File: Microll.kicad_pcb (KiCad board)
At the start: 2 copper layers, 22 parts, among them J1 USB_C_Receptacle, U1 ESP32-C3-WROOM-02-N4, U2 TLV76733DRVx, U3 STM32G0B1CBU6, U4 USBLC6-2P6, U5 DPDT_Switch_x2, U6 LSM6DSL

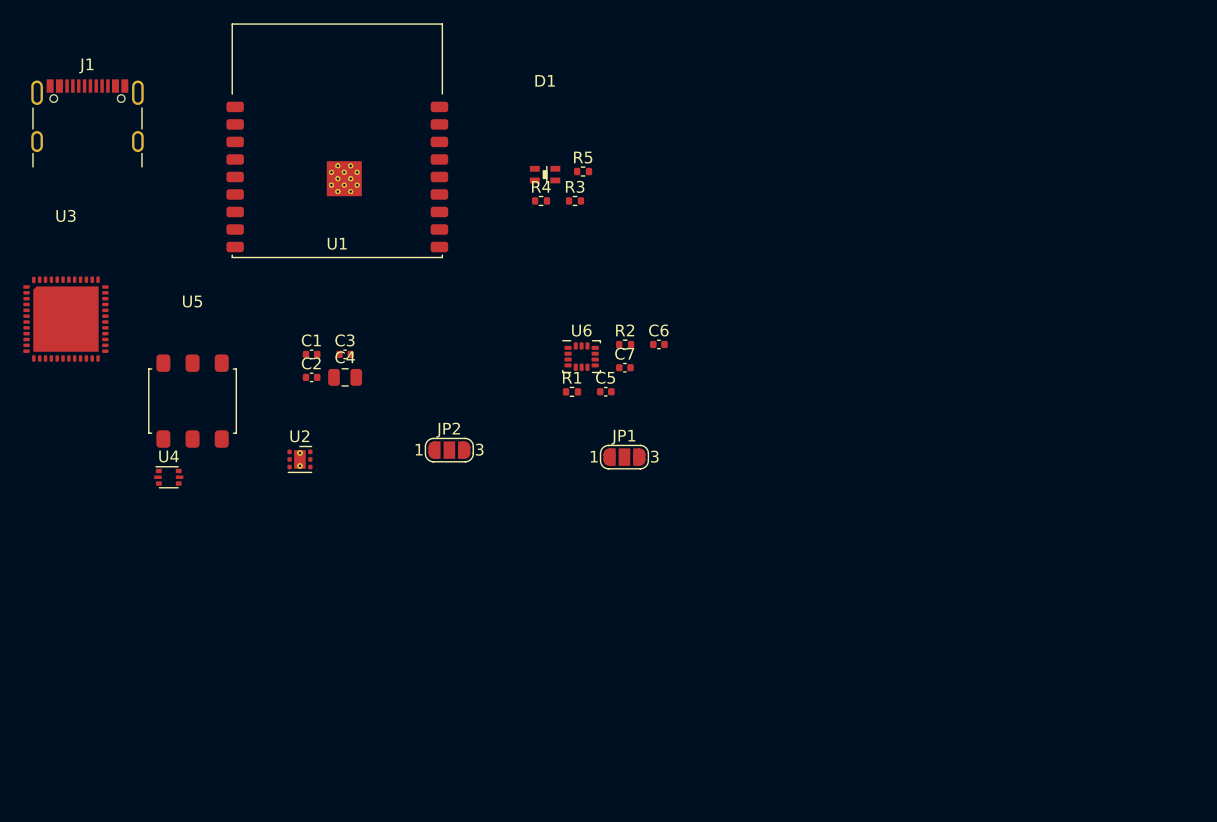
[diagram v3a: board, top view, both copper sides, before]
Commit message: Added I/O connections
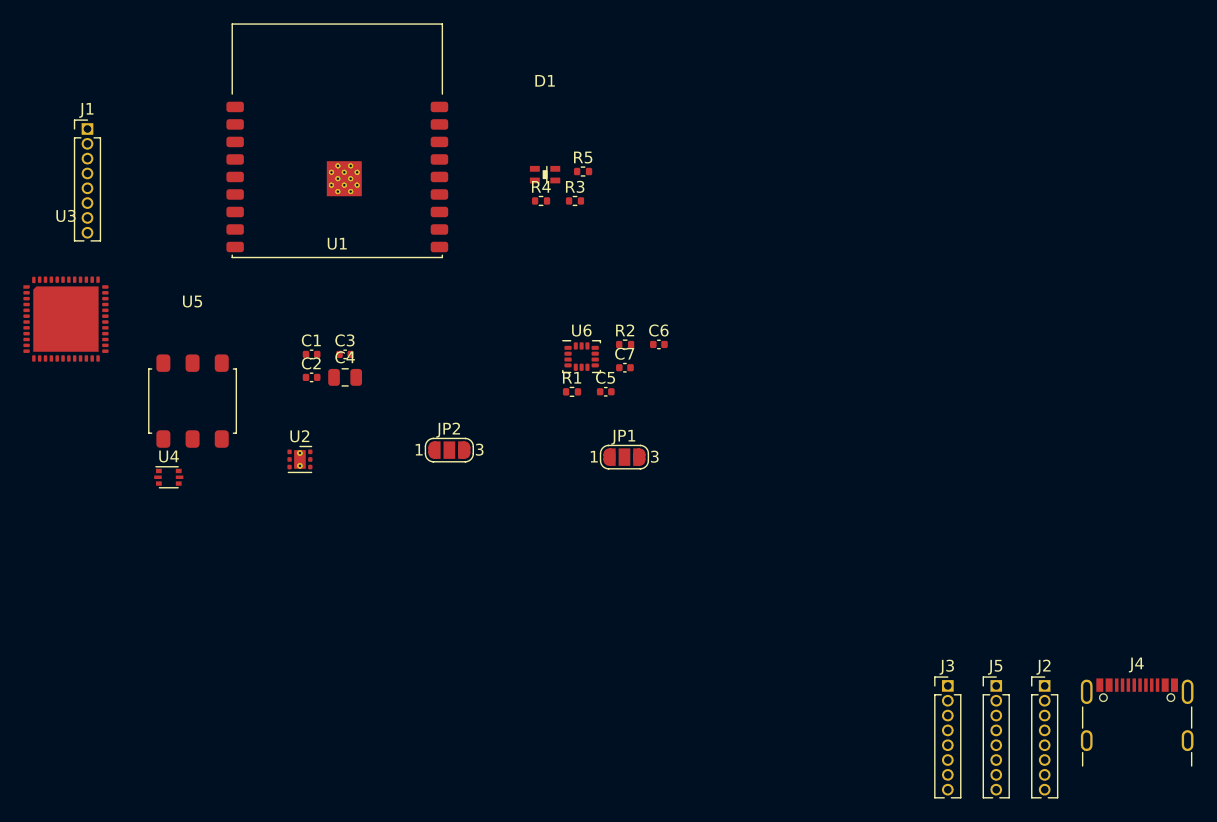
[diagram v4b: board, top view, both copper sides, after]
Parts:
- added J2: Conn_01x08, Connector_PinHeader_1.27mm:PinHeader_1x08_P1.27mm_Vertical, F.Cu at (222.0, 122.8)
- added J3: Conn_01x08, Connector_PinHeader_1.27mm:PinHeader_1x08_P1.27mm_Vertical, F.Cu at (213.7, 122.8)
- added J4: USB_C_Receptacle, Connector_USB:USB_C_Receptacle_GCT_USB4105-xx-A_16P_TopMnt_Horizontal, F.Cu at (229.9, 126.4)
- added J5: Conn_01x08, Connector_PinHeader_1.27mm:PinHeader_1x08_P1.27mm_Vertical, F.Cu at (217.8, 122.8)
- J1: value USB_C_Receptacle -> Conn_01x08; footprint Connector_USB:USB_C_Receptacle_GCT_USB4105-xx-A_16P_TopMnt_Horizontal -> Connector_PinHeader_1.27mm:PinHeader_1x08_P1.27mm_Vertical
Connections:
- U1 pad 10: unconnected-(U1-Pad10) -> /GPIO10
- U1 pad 11: unconnected-(U1-Pad11) -> /Rx
- U1 pad 12: unconnected-(U1-Pad12) -> /Tx
- U1 pad 15: unconnected-(U1-Pad15) -> /GPIO3
- U1 pad 16: unconnected-(U1-Pad16) -> /GPIO2
- U1 pad 17: unconnected-(U1-Pad17) -> /GPIO1
- U1 pad 18: unconnected-(U1-Pad18) -> /Blue
- U1 pad 6: unconnected-(U1-Pad6) -> /GPIO7
- U1 pad 7: unconnected-(U1-Pad7) -> /GPIO8
- U3 pad 13: unconnected-(U3-Pad13) -> /PA2
- U3 pad 14: unconnected-(U3-Pad14) -> /PA3
- U3 pad 19: unconnected-(U3-Pad19) -> /PB0
- U3 pad 20: unconnected-(U3-Pad20) -> /PB1
- U3 pad 25: unconnected-(U3-Pad25) -> /PB13
- U3 pad 26: unconnected-(U3-Pad26) -> /PB14
- U3 pad 27: unconnected-(U3-Pad27) -> /PB15
- U3 pad 28: unconnected-(U3-Pad28) -> /PA8
- U3 pad 41: unconnected-(U3-Pad41) -> /PD3
- U3 pad 42: unconnected-(U3-Pad42) -> /PB3
- U3 pad 43: unconnected-(U3-Pad43) -> /PB4
- U3 pad 44: unconnected-(U3-Pad44) -> /PB5

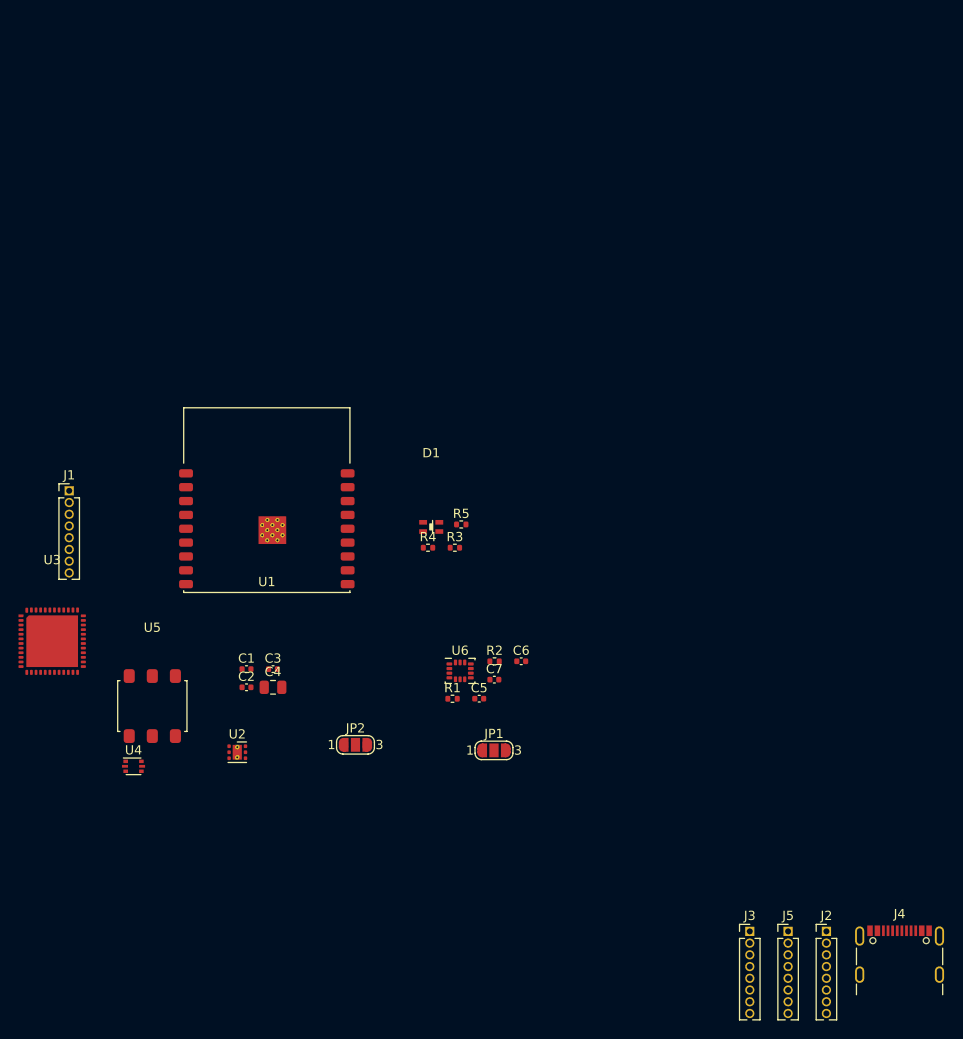
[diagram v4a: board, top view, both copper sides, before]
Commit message: Initial placement for the PCB.
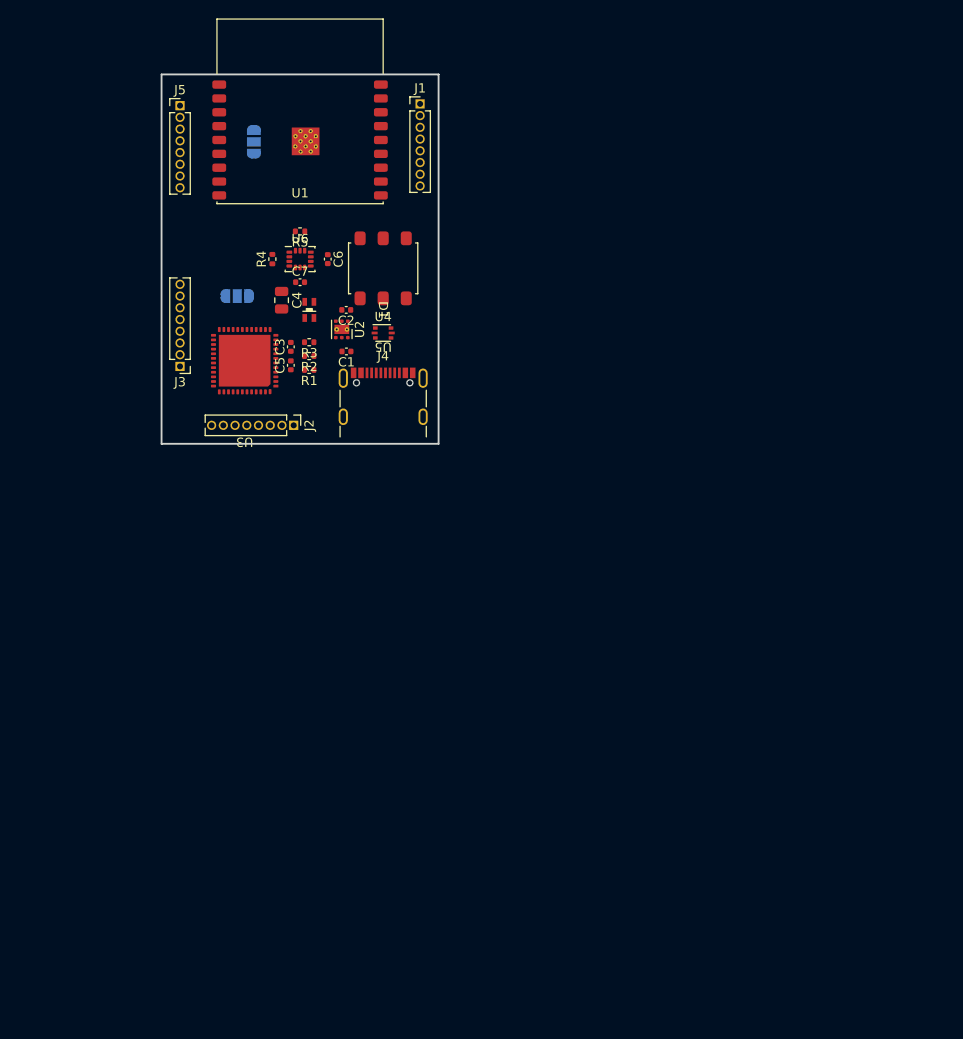
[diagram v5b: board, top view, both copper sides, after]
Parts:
- JP1, JP2: moved to B.Cu
- moved J5 111.1 mm to (152.0, 33.4)
- moved J3 86.9 mm to (152.0, 61.6), turned to 180 degrees
- moved J4 82.3 mm to (174.0, 66.0)
- moved J2 79.6 mm to (164.3, 68.0), turned to -90 degrees
- moved JP1 70.8 mm to (160.0, 37.3), turned to -90 degrees
- moved J1 56.6 mm to (178.0, 33.2)
- moved U4 54.2 mm to (174.0, 58.0)
- moved U5 53.6 mm to (174.0, 51.0), turned to 180 degrees
- moved JP2 50.3 mm to (158.2, 54.0)
- moved C6 48.3 mm to (168.0, 50.0), turned to -90 degrees
- moved C7 47.9 mm to (165.0, 52.5)
- moved U6 47.8 mm to (165.0, 50.0)
- moved U2 47.2 mm to (169.5, 57.6), turned to -90 degrees
- moved C2 42.3 mm to (170.0, 55.5), turned to 180 degrees
- moved U1 42.3 mm to (165.0, 37.1)
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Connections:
- JP2 pad 2: Net-(JP2-Pad2) -> Net-(JP2-C)
- U3 pad 35: (no net) -> Net-(JP2-C)
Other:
- board outline added: 30 x 40 mm

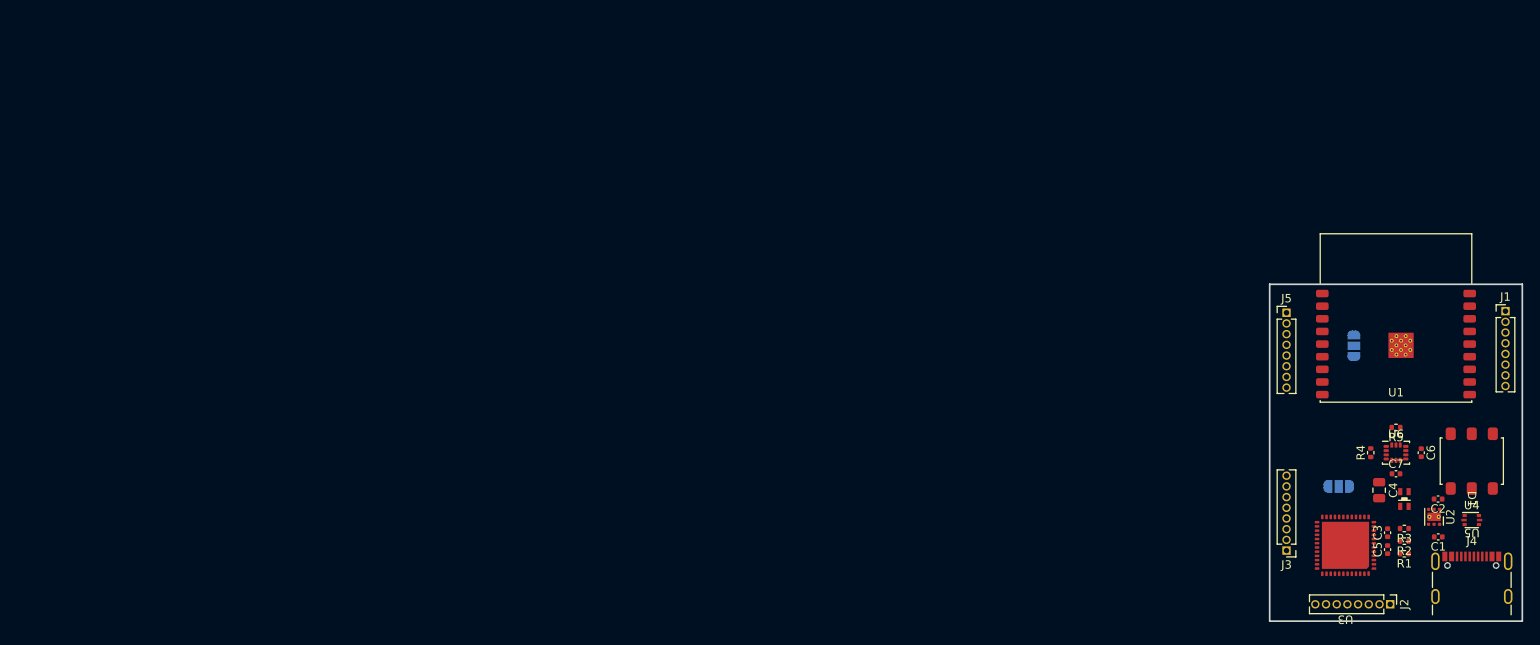
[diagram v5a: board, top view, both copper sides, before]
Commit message: Updated STMew and ESP32 symbols with correct pins. Need to update USB-C next.
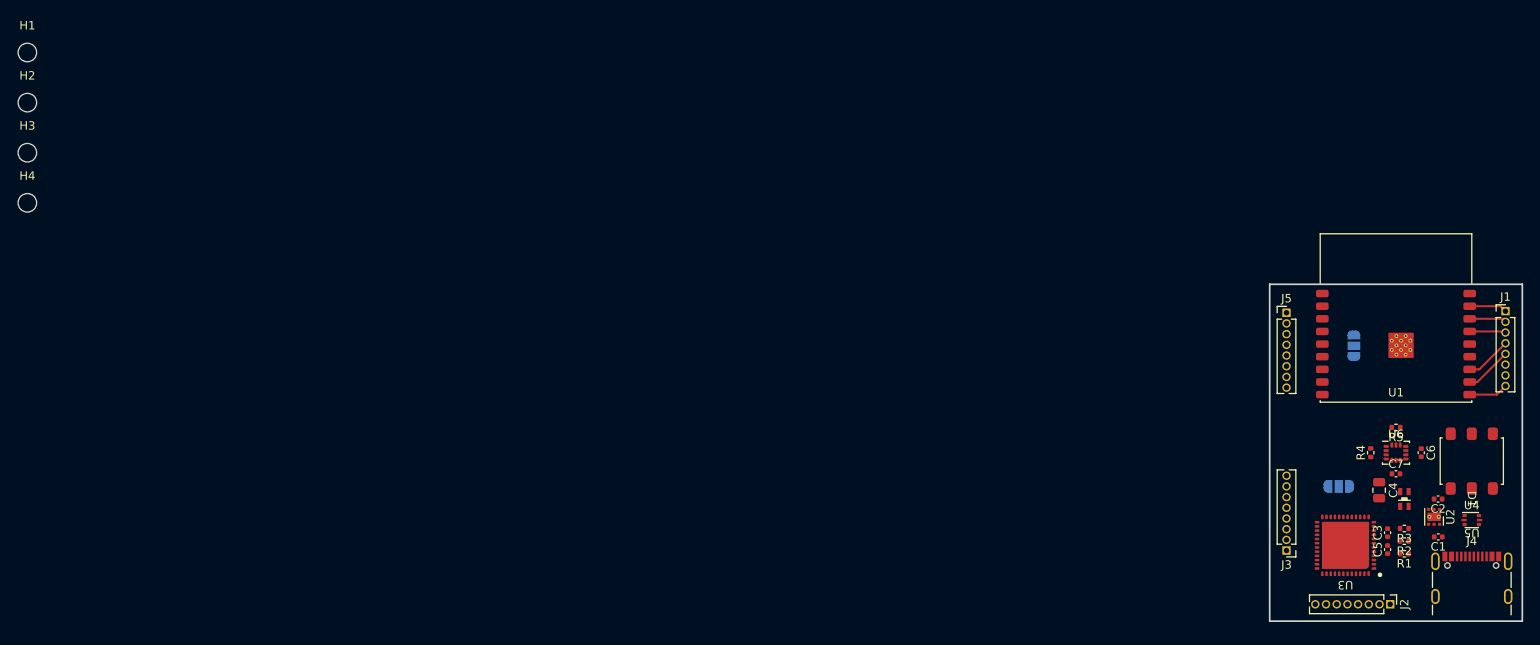
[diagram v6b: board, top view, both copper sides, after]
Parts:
- added H1: MountingHole, MountingHole:MountingHole_2.2mm_M2, F.Cu at (2.48, 2.48)
- added H2: MountingHole, MountingHole:MountingHole_2.2mm_M2, F.Cu at (2.48, 8.43)
- added H3: MountingHole, MountingHole:MountingHole_2.2mm_M2, F.Cu at (2.48, 14.4)
- added H4: MountingHole, MountingHole:MountingHole_2.2mm_M2, F.Cu at (2.48, 20.3)
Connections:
- U1 pad 3: (no net) -> SDA
- U1 pad TP: (no net) -> unconnected-(U1-PadTP)
- U3 pad 36: (no net) -> unconnected-(U3-PA14-BOOT0-Pad36)
- U3 pad TP: (no net) -> GND
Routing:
- net /Rx: track 0.00 -> 5.63 mm
- net /Tx: track 0.00 -> 5.53 mm
- net /GPIO10: track 0.00 -> 4.67 mm
- net /GPIO1: track 0.00 -> 4.49 mm
- net /GPIO2: track 0.00 -> 4.40 mm
- net /GPIO3: track 0.00 -> 4.30 mm

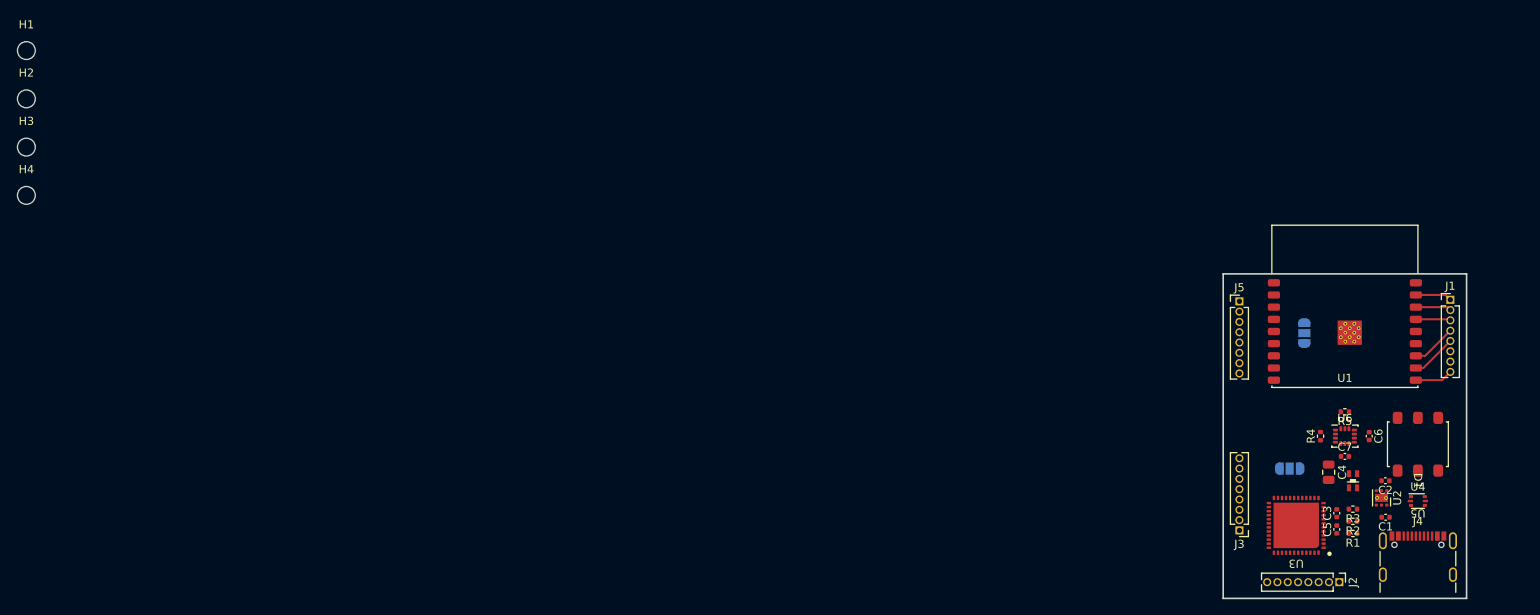
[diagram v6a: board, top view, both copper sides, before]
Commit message: USB-C footprint should now match schematic
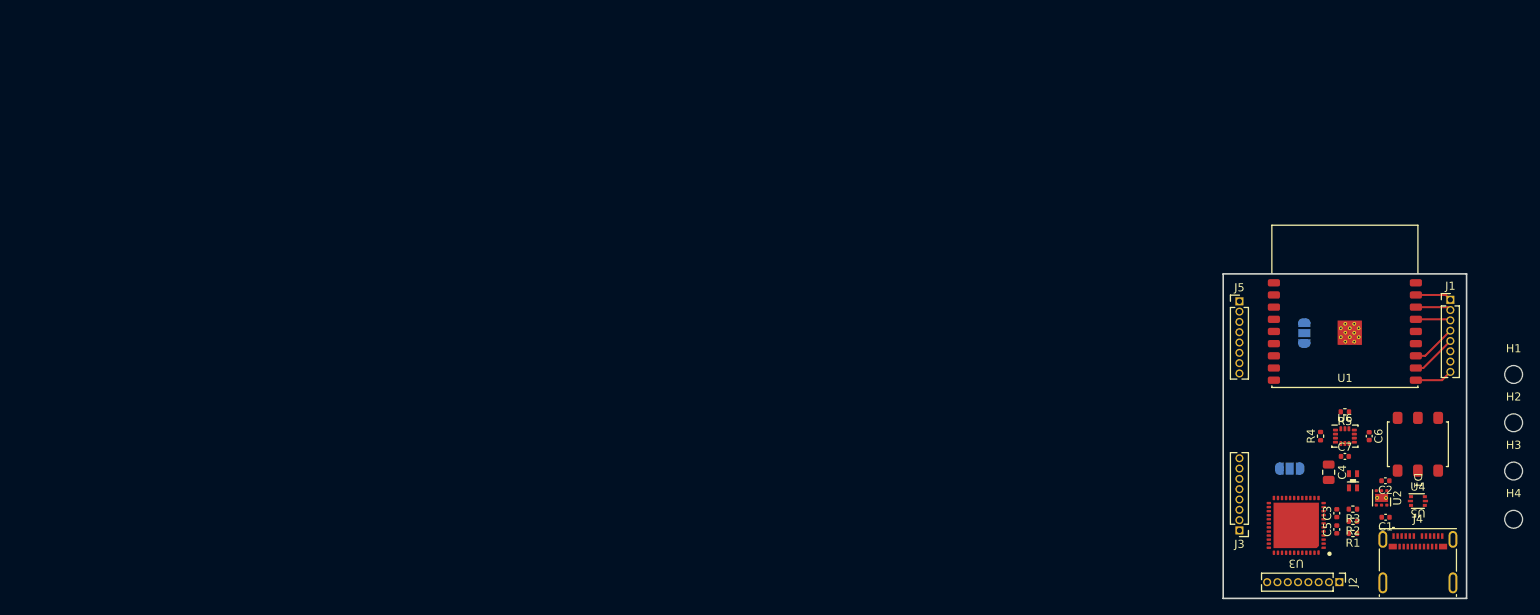
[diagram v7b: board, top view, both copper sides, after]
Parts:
- J4: footprint Connector_USB:USB_C_Receptacle_GCT_USB4105-xx-A_16P_TopMnt_Horizontal -> Connector_USB:USB_C_Receptacle_Molex_105450-0101
- moved H1 187.6 mm to (185.8, 42.4)
- moved H2 187.6 mm to (185.8, 48.4)
- moved H3 187.6 mm to (185.8, 54.3)
- moved H4 187.6 mm to (185.8, 60.2)
- moved J4 0.47 mm to (174.0, 65.5)
